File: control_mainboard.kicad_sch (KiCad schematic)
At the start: 50 parts, among them J1 USB_C_Receptacle_USB2.0_14P, J2 [battery connector], J3 SD_Card_Receptacle, J4 [bootstrap jumper], Q1 DMG3415, Q2 DMG3415, SW1 [reset button], SW5 SW_SPST, U1 RP2040, U2 XC6220B331MR, U3 MCP73831-2-OT, U4 W25Q128JVS, Y1 ABM8-272-T3

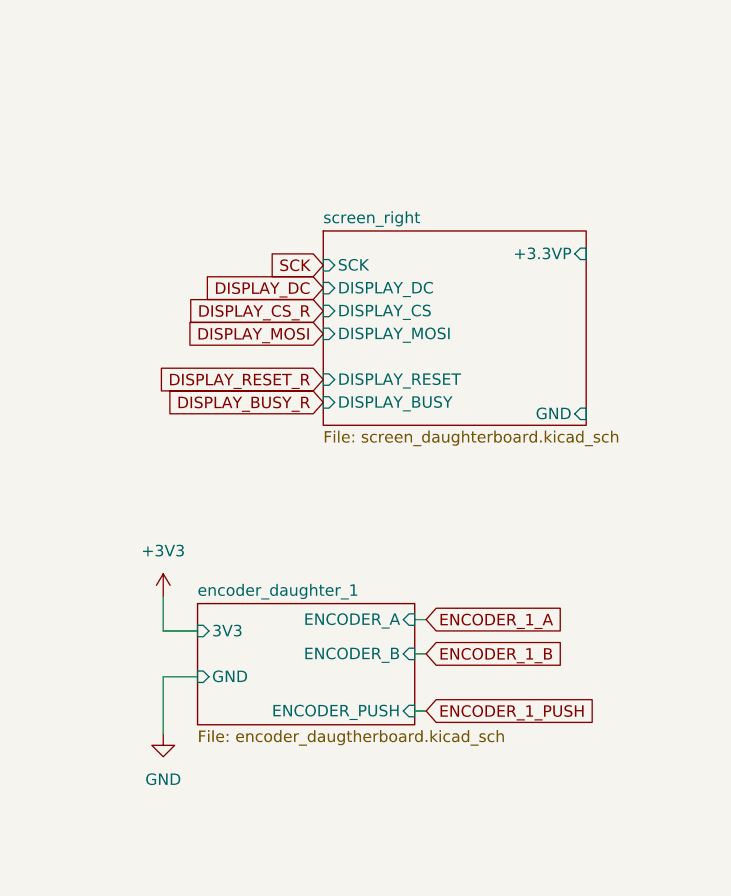
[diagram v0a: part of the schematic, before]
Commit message: fixed page numbers
and adjusted some label types
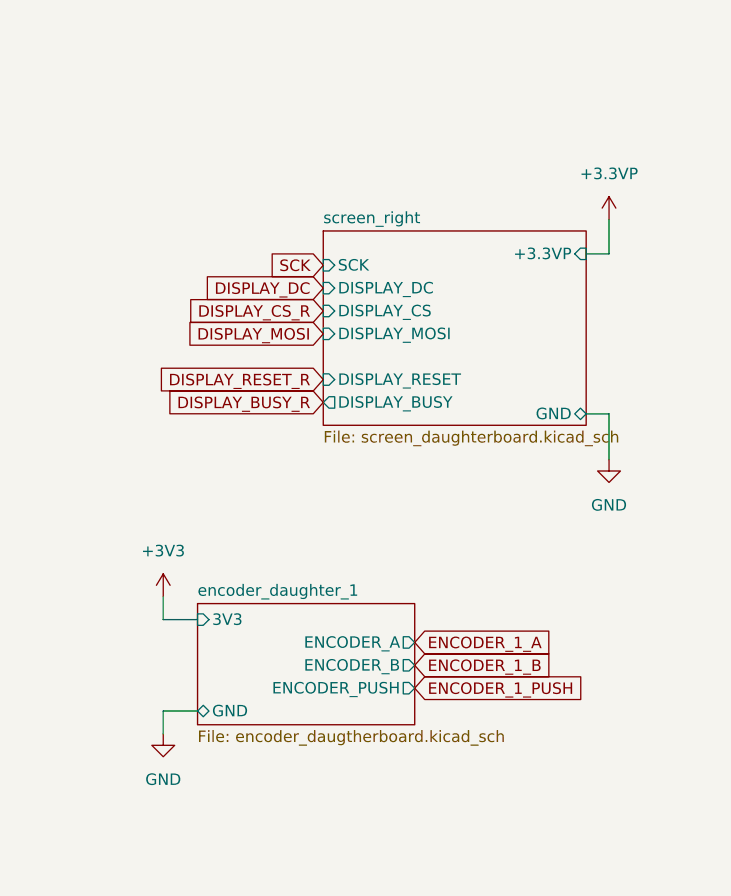
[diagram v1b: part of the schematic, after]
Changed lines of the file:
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@@
 	(wire
 		(pts
-			(xy 219.71 107.95) (xy 219.71 111.76)
+			(xy 219.71 107.95) (xy 219.71 110.49)
 		)
 		(stroke
@@
 	(wire
 		(pts
-			(xy 62.23 68.58) (xy 62.23 81.28)
+			(xy 269.24 87.63) (xy 269.24 92.71)
 		)
 		(stroke
@@
 	(wire
 		(pts
-			(xy 120.65 35.56) (xy 120.65 46.99)
+			(xy 62.23 68.58) (xy 62.23 81.28)
 		)
 		(stroke
@@
 	(wire
 		(pts
-			(xy 247.65 120.65) (xy 248.92 120.65)
+			(xy 120.65 35.56) (xy 120.65 46.99)
 		)
 		(stroke
@@
 	(wire
 		(pts
-			(xy 247.65 110.49) (xy 248.92 110.49)
-		)
-		(stroke
-			(width 0)
-			(type default)
-		)
-	)
-	(wire
-		(pts
 			(xy 66.04 194.31) (xy 45.72 194.31)
 		)
@@
 	(wire
 		(pts
-			(xy 219.71 116.84) (xy 223.52 116.84)
-		)
-		(stroke
-			(width 0)
-			(type default)
-		)
-	)
-	(wire
-		(pts
 			(xy 120.65 33.02) (xy 120.65 35.56)
 		)
@@
 	(wire
 		(pts
-			(xy 219.71 123.19) (xy 219.71 116.84)
-		)
-		(stroke
-			(width 0)
-			(type default)
-		)
-	)
-	(wire
-		(pts
 			(xy 133.35 193.04) (xy 132.08 193.04)
 		)
@@
 	(wire
 		(pts
+			(xy 266.7 69.85) (xy 269.24 69.85)
+		)
+		(stroke
+			(width 0)
+			(type default)
+		)
+	)
+	(wire
+		(pts
 			(xy 46.99 200.66) (xy 48.26 200.66)
 		)
@@
 	(wire
 		(pts
-			(xy 247.65 114.3) (xy 248.92 114.3)
+			(xy 26.67 226.06) (xy 26.67 227.33)
 		)
 		(stroke
@@
 	(wire
 		(pts
-			(xy 26.67 226.06) (xy 26.67 227.33)
+			(xy 160.02 80.01) (xy 158.75 80.01)
 		)
 		(stroke
@@
 	(wire
 		(pts
-			(xy 160.02 80.01) (xy 158.75 80.01)
+			(xy 72.39 90.17) (xy 85.09 90.17)
 		)
 		(stroke
@@
 	(wire
 		(pts
-			(xy 72.39 90.17) (xy 85.09 90.17)
+			(xy 269.24 69.85) (xy 269.24 66.04)
 		)
 		(stroke
@@
 	(wire
 		(pts
-			(xy 219.71 111.76) (xy 223.52 111.76)
+			(xy 219.71 110.49) (xy 223.52 110.49)
+		)
+		(stroke
+			(width 0)
+			(type default)
+		)
+	)
+	(wire
+		(pts
+			(xy 266.7 87.63) (xy 269.24 87.63)
 		)
 		(stroke
@@
 	(wire
 		(pts
+			(xy 219.71 120.65) (xy 219.71 123.19)
+		)
+		(stroke
+			(width 0)
+			(type default)
+		)
+	)
+	(wire
+		(pts
 			(xy 68.58 201.93) (xy 68.58 226.06)
 		)
@@
 	(wire
 		(pts
+			(xy 219.71 120.65) (xy 223.52 120.65)
+		)
+		(stroke
+			(width 0)
+			(type default)
+		)
+	)
+	(wire
+		(pts
 			(xy 99.06 267.97) (xy 99.06 271.78)
 		)
@@
 	(global_label "ENCODER_1_B"
 		(shape input)
-		(at 248.92 114.3 0)
+		(at 247.65 115.57 0)
 		(fields_autoplaced yes)
 		(effects
@@
 		)
 		(property "Intersheetrefs" "${INTERSHEET_REFS}"
-			(at 265.0889 114.3 0)
+			(at 263.8189 115.57 0)
 			(effects
 				(font
@@
 	(global_label "ENCODER_1_PUSH"
 		(shape input)
-		(at 248.92 120.65 0)
+		(at 247.65 118.11 0)
 		(fields_autoplaced yes)
 		(effects
@@
 		)
 		(property "Intersheetrefs" "${INTERSHEET_REFS}"
-			(at 268.9594 120.65 0)
+			(at 267.6894 118.11 0)
 			(effects
 				(font
@@
 	(global_label "ENCODER_1_A"
 		(shape input)
-		(at 248.92 110.49 0)
+		(at 247.65 113.03 0)
 		(fields_autoplaced yes)
 		(effects
@@
 		)
 		(property "Intersheetrefs" "${INTERSHEET_REFS}"
-			(at 264.9075 110.49 0)
+			(at 263.6375 113.03 0)
 			(effects
 				(font
@@
 	)
 	(symbol
+		(lib_id "power:GND")
+		(at 269.24 92.71 0)
+		(unit 1)
+		(exclude_from_sim no)
+		(in_bom yes)
+		(on_board yes)
+		(dnp no)
+		(fields_autoplaced yes)
+		(property "Reference" "#PWR0107"
+			(at 269.24 99.06 0)
+			(effects
+				(font
+					(size 1.27 1.27)
+				)
+				(hide yes)
+			)
+		)
+		(property "Value" "GND"
+			(at 269.24 97.79 0)
+			(effects
+				(font
+					(size 1.27 1.27)
+				)
+			)
+		)
+		(property "Footprint" ""
+			(at 269.24 92.71 0)
+			(effects
+				(font
+					(size 1.27 1.27)
+				)
+				(hide yes)
+			)
+		)
+		(property "Datasheet" ""
+			(at 269.24 92.71 0)
+			(effects
+				(font
+					(size 1.27 1.27)
+				)
+				(hide yes)
+			)
+		)
+		(property "Description" "Power symbol creates a global label with name \"GND\" , ground"
+			(at 269.24 92.71 0)
+			(effects
+				(font
+					(size 1.27 1.27)
+				)
+				(hide yes)
+			)
+		)
+		(pin "1"
+		)
+		(instances
+			(project "Tome"
+				(path "/2c6baa8c-bfd7-43e4-8688-255743ea3ca6/70ad74b6-7d6e-42de-a92a-6cae4a86bd4c"
+					(reference "#PWR0107")
+					(unit 1)
+				)
+			)
+		)
+	)
+	(symbol
 		(lib_id "power:+4V")
 		(at 88.9 177.8 0)
@@
 	)
 	(symbol
+		(lib_id "power:+3.3VP")
+		(at 269.24 66.04 0)
+		(unit 1)
+		(exclude_from_sim no)
+		(in_bom yes)
+		(on_board yes)
+		(dnp no)
+		(fields_autoplaced yes)
+		(property "Reference" "#PWR0102"
+			(at 273.05 67.31 0)
+			(effects
+				(font
+					(size 1.27 1.27)
+				)
+				(hide yes)
+			)
+		)
+		(property "Value" "+3.3VP"
+			(at 269.24 60.96 0)
+			(effects
+				(font
+					(size 1.27 1.27)
+				)
+			)
+		)
+		(property "Footprint" ""
+			(at 269.24 66.04 0)
+			(effects
+				(font
+					(size 1.27 1.27)
+				)
+				(hide yes)
+			)
+		)
+		(property "Datasheet" ""
+			(at 269.24 66.04 0)
+			(effects
+				(font
+					(size 1.27 1.27)
+				)
+				(hide yes)
+			)
+		)
+		(property "Description" "Power symbol creates a global label with name \"+3.3VP\""
+			(at 269.24 66.04 0)
+			(effects
+				(font
+					(size 1.27 1.27)
+				)
+				(hide yes)
+			)
+		)
+		(pin "1"
+		)
+		(instances
+			(project "Tome"
+				(path "/2c6baa8c-bfd7-43e4-8688-255743ea3ca6/70ad74b6-7d6e-42de-a92a-6cae4a86bd4c"
+					(reference "#PWR0102")
+					(unit 1)
+				)
+			)
+		)
+	)
+	(symbol
 		(lib_id "power:GND")
 		(at 68.58 67.31 0)
@@
 			)
 		)
-		(pin "DISPLAY_BUSY" input
-			(at 237.49 86.36 180)
-			(effects
-				(font
-					(size 1.27 1.27)
-				)
-				(justify left)
-			)
-		)
 		(pin "DISPLAY_RESET" input
 			(at 237.49 83.82 180)
@@
 			)
 		)
-		(pin "GND" input
+		(pin "DISPLAY_BUSY" output
+			(at 237.49 86.36 180)
+			(effects
+				(font
+					(size 1.27 1.27)
+				)
+				(justify left)
+			)
+		)
+		(pin "GND" bidirectional
 			(at 266.7 87.63 0)
 			(effects
@@
 			(project "Tome"
 				(path "/2c6baa8c-bfd7-43e4-8688-255743ea3ca6/70ad74b6-7d6e-42de-a92a-6cae4a86bd4c"
-					(page "5")
+					(page "4")
 				)
 			)
@@
 			)
 		)
-		(pin "ENCODER_A" input
-			(at 247.65 110.49 0)
+		(pin "3V3" input
+			(at 223.52 110.49 180)
 			(effects
 				(font
 					(size 1.27 1.27)
 				)
-				(justify right)
+				(justify left)
 			)
 		)
-		(pin "ENCODER_B" input
-			(at 247.65 114.3 0)
+		(pin "ENCODER_PUSH" output
+			(at 247.65 118.11 0)
 			(effects
 				(font
@@
 			)
 		)
-		(pin "ENCODER_PUSH" input
-			(at 247.65 120.65 0)
+		(pin "ENCODER_A" output
+			(at 247.65 113.03 0)
 			(effects
 				(font
@@
 			)
 		)
-		(pin "3V3" input
-			(at 223.52 111.76 180)
+		(pin "ENCODER_B" output
+			(at 247.65 115.57 0)
 			(effects
 				(font
 					(size 1.27 1.27)
 				)
-				(justify left)
+				(justify right)
 			)
 		)
-		(pin "GND" input
-			(at 223.52 116.84 180)
+		(pin "GND" bidirectional
+			(at 223.52 120.65 180)
 			(effects
 				(font
@@
 			(project "Tome"
 				(path "/2c6baa8c-bfd7-43e4-8688-255743ea3ca6/70ad74b6-7d6e-42de-a92a-6cae4a86bd4c"
-					(page "2")
+					(page "6")
 				)
 			)

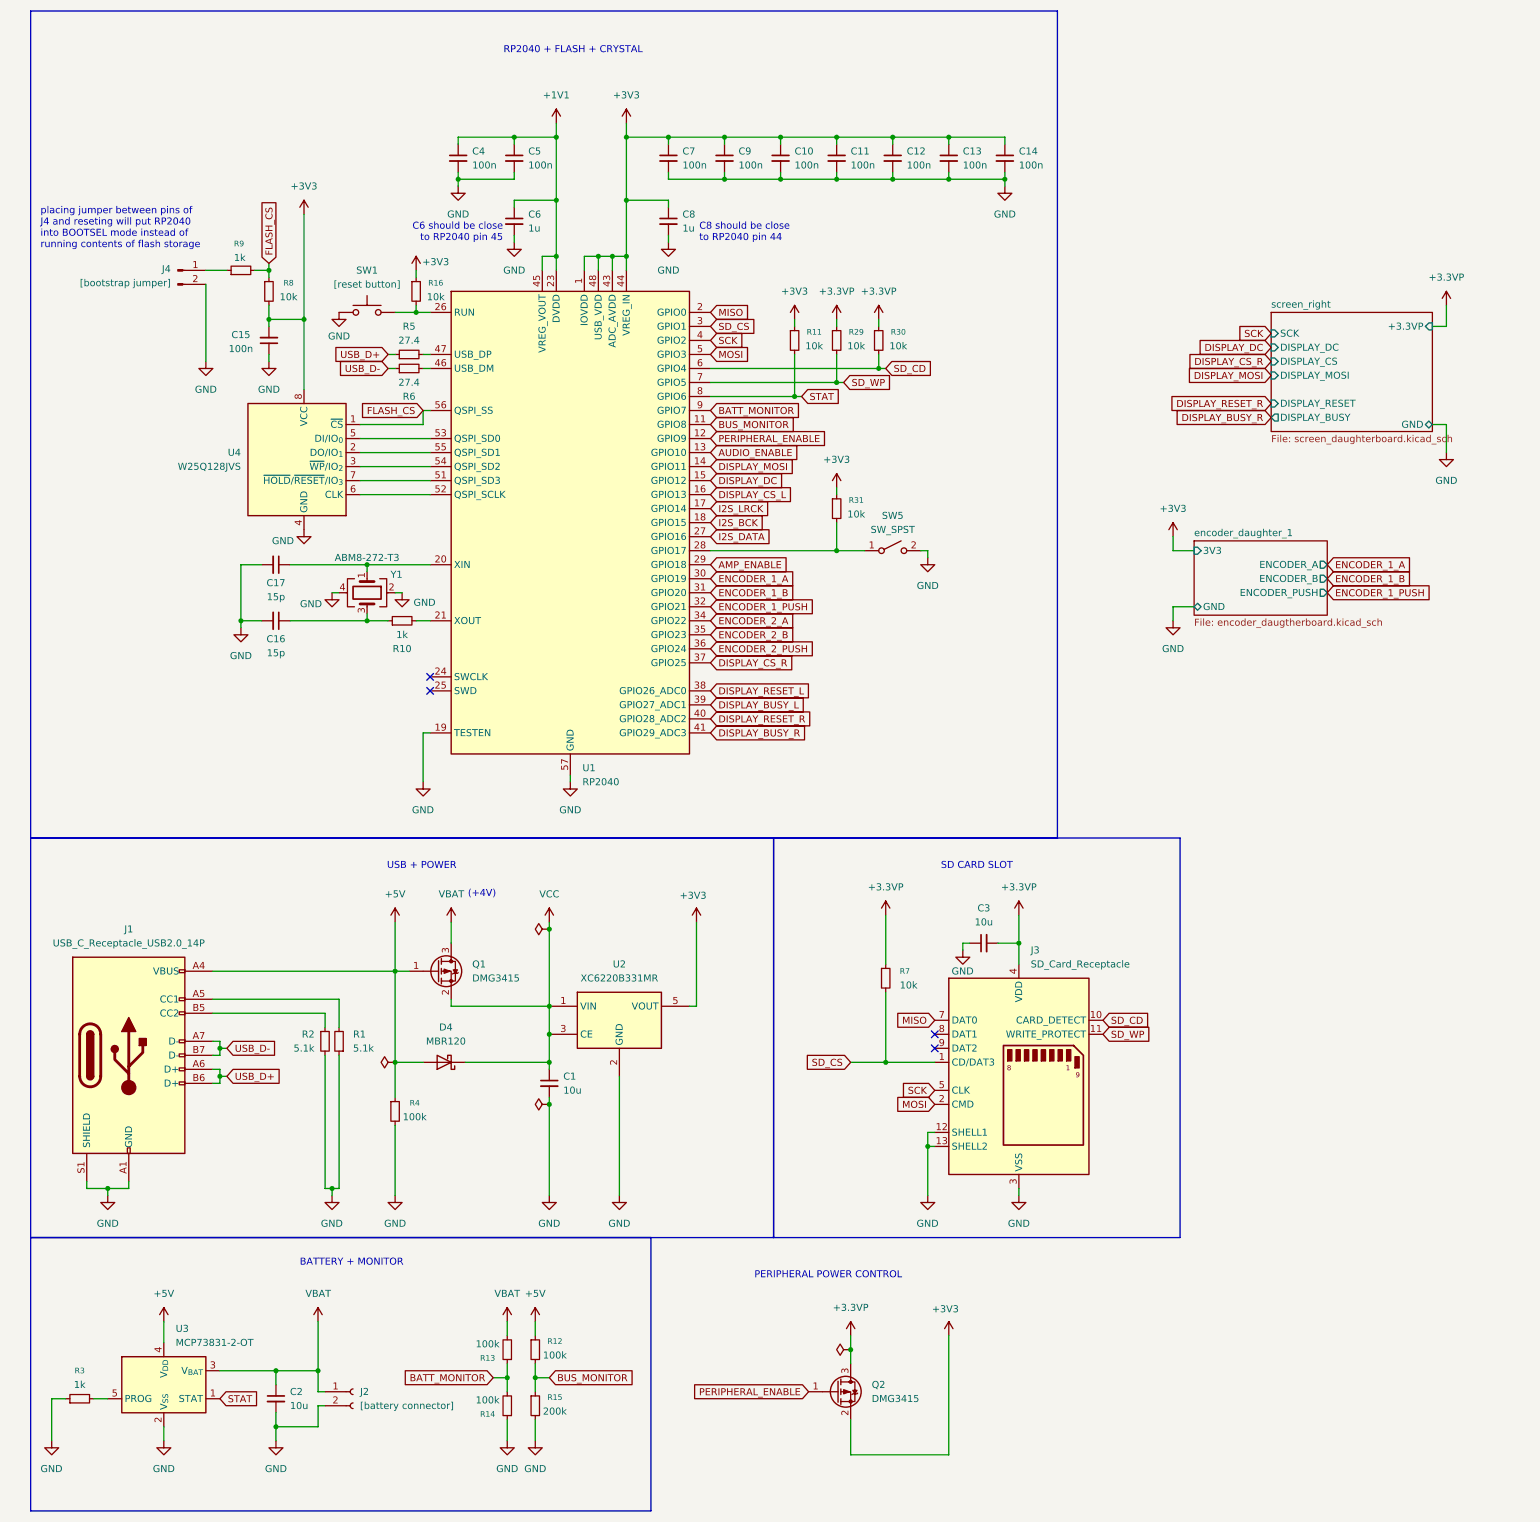
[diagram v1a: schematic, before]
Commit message: separating schematics based on board
finished splitting every component up into separate sheets in the schematic based on what physical board it's going on
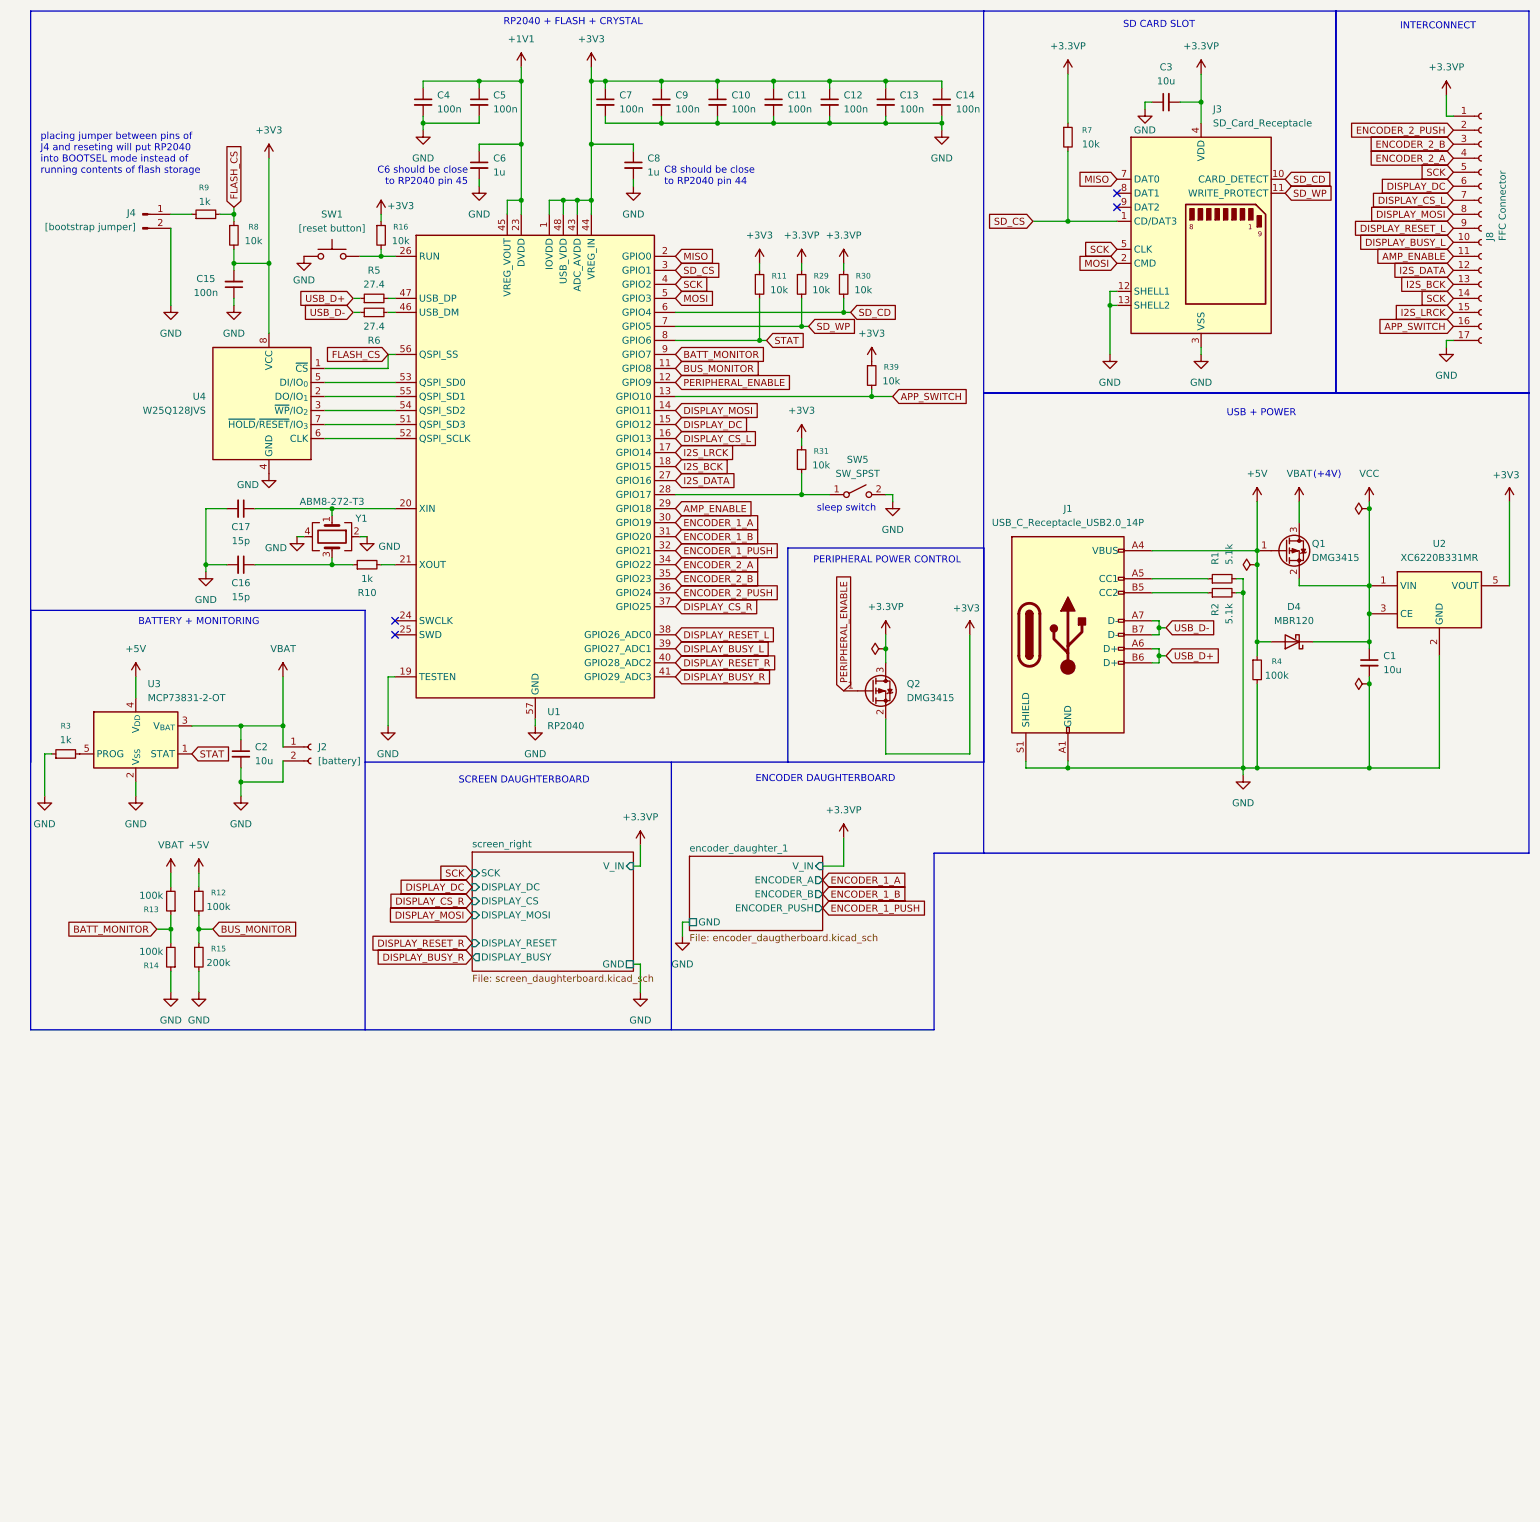
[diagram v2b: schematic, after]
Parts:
- added J8: FFC Connector, symbol Connector:Conn_01x17_Socket
- added R39: 10k, symbol Device:R_Small
- J2: value [battery connector] -> [battery]
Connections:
- net +3.3VP: now also J8.1 (Pin_1)
- net +3V3: now also R39.1
- net AMP_ENABLE: now also J8.11 (Pin_11)
- net DISPLAY_BUSY_L: now also J8.10 (Pin_10)
- net DISPLAY_CS_L: now also J8.7 (Pin_7)
- net DISPLAY_DC: now also J8.6 (Pin_6)
- net DISPLAY_MOSI: now also J8.8 (Pin_8)
- net DISPLAY_RESET_L: now also J8.9 (Pin_9)
- net ENCODER_2_A: now also J8.4 (Pin_4)
- net ENCODER_2_B: now also J8.3 (Pin_3)
- net ENCODER_2_PUSH: now also J8.2 (Pin_2)
- net GND: now also R1.2, J8.17 (Pin_17); no longer R1.1
- net I2S_BCK: now also J8.13 (Pin_13)
- net I2S_DATA: now also J8.12 (Pin_12)
- net I2S_LRCK: now also J8.15 (Pin_15)
- net SCK: now also J8.14 (Pin_14), J8.5 (Pin_5)
- net at J1.A5 (CC1): now also R1.1; no longer R1.2
- net AUDIO_ENABLE renamed APP_SWITCH
- net APP_SWITCH: now also J8.16 (Pin_16), R39.2
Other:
- sheet encoder_daughter_1 ports: added V_IN; removed 3V3
- sheet screen_right ports: added V_IN; removed +3.3VP
- note added: "BATTERY + MONITORING"
- note added: "ENCODER DAUGHTERBOARD"
- note added: "INTERCONNECT"
- note added: "SCREEN DAUGHTERBOARD"
- note added: "sleep switch"
- note removed: "BATTERY + MONITOR"
- moved on the sheet: C1, C10, C11, C12, C13, C14, C15, C16, C17, C2, C3, C4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
